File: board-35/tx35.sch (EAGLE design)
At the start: 23 parts, among them J1 SWD_SHROUD, Q1 MOSFET-NCHANNEL2N7002PW, X1 SMA-142-0711-821/826

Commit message: almost done 35mhz tranasmitter
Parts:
- added C13: (no value), passives-7351:CAPACITOR0805-N
- added JP1: (no value), Mine:M02PTH
- added JP2: (no value), SparkFun-Connectors:M06SILK_FEMALE_PTH
- added R4: 10k, passives-7351:RESISTOR0603-N
- IC1: value STM32F0-32 -> STM32F030K6
- renumbered U$1 to IC1
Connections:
- new net N$12: IC1.PA9, JP2.5
- new net N$13: IC1.BOOT0, JP1.1, R4.P$1
- new net N$7: C13.1, JP2.2, L1.P$2
- new net N$9: IC1.PA10, JP2.4
- net +3V3: now also JP1.2, JP2.3
- net GND: now also C13.2, JP2.1, R4.P$2
- net N$5: now also JP2.6
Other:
- note added: "analogue in/out"
- note added: "control in"
- note added: "en"
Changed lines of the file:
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@@
 <?xml version="1.0" encoding="utf-8"?>
 <!DOCTYPE eagle SYSTEM "eagle.dtd">
-<eagle version="6.5.0">
+<eagle version="6.6.0">
 <drawing>
 <settings>
@@
 </classes>
 <parts>
-<part name="U$1" library="Mine" deviceset="STM32F0-32" device=""/>
+<part name="IC1" library="Mine" deviceset="STM32F0-32" device="" value="STM32F030K6"/>
 <part name="Y1" library="SparkFun-FreqCtrl" deviceset="CRYSTAL" device="HC49UV"/>
 <part name="C1" library="passives-7351" deviceset="CAPACITOR" device="0603-N" value="18p"/>
@@
 <part name="GND10" library="supply1" deviceset="GND" device=""/>
 <part name="GND11" library="supply1" deviceset="GND" device=""/>
+<part name="+3V3" library="supply1" deviceset="+3V3" device=""/>
+<part name="GND12" library="supply1" deviceset="GND" device=""/>
+<part name="JP2" library="SparkFun-Connectors" deviceset="M06" device="SILK_FEMALE_PTH"/>
+<part name="R4" library="passives-7351" deviceset="RESISTOR" device="0603-N" value="10k"/>
+<part name="GND13" library="supply1" deviceset="GND" device=""/>
+<part name="JP1" library="Mine" deviceset="M02" device="PTH"/>
+<part name="+3V4" library="supply1" deviceset="+3V3" device=""/>
+<part name="C13" library="passives-7351" deviceset="CAPACITOR" device="0805-N"/>
+<part name="GND14" library="supply1" deviceset="GND" device=""/>
 </parts>
 <sheets>
@@
 <text x="114.3" y="66.04" size="1.778" layer="91">CHECK</text>
 <text x="104.14" y="60.96" size="1.778" layer="91">CHECK</text>
+<text x="78.74" y="139.7" size="1.778" layer="91">analogue in/out</text>
+<text x="78.74" y="134.62" size="1.778" layer="91">control in</text>
+<text x="78.74" y="137.16" size="1.778" layer="91">en</text>
 </plain>
 <instances>
-<instance part="U$1" gate="G$1" x="50.8" y="25.4"/>
+<instance part="IC1" gate="G$1" x="50.8" y="25.4"/>
 <instance part="Y1" gate="G$1" x="96.52" y="10.16" rot="R180"/>
 <instance part="C1" gate="G$1" x="91.44" y="2.54"/>
@@
 <instance part="GND10" gate="1" x="175.26" y="55.88"/>
 <instance part="GND11" gate="1" x="187.96" y="58.42"/>
+<instance part="+3V3" gate="G$1" x="76.2" y="132.08" rot="R270"/>
+<instance part="GND12" gate="1" x="76.2" y="121.92"/>
+<instance part="JP2" gate="G$1" x="68.58" y="132.08"/>
+<instance part="R4" gate="G$1" x="10.16" y="48.26" rot="R270"/>
+<instance part="GND13" gate="1" x="10.16" y="40.64"/>
+<instance part="JP1" gate="G$1" x="-10.16" y="53.34"/>
+<instance part="+3V4" gate="G$1" x="0" y="55.88" rot="R270"/>
+<instance part="C13" gate="G$1" x="127" y="88.9"/>
+<instance part="GND14" gate="1" x="127" y="81.28"/>
 </instances>
 <busses>
@@
 <net name="N$1" class="0">
 <segment>
-<pinref part="U$1" gate="G$1" pin="PF1"/>
+<pinref part="IC1" gate="G$1" pin="PF1"/>
 <wire x1="83.82" y1="10.16" x2="88.9" y2="10.16" width="0.1524" layer="91"/>
 <wire x1="88.9" y1="10.16" x2="88.9" y2="15.24" width="0.1524" layer="91"/>
@@
 <net name="N$2" class="0">
 <segment>
-<pinref part="U$1" gate="G$1" pin="PF0"/>
+<pinref part="IC1" gate="G$1" pin="PF0"/>
 <pinref part="C1" gate="G$1" pin="1"/>
 <wire x1="83.82" y1="12.7" x2="91.44" y2="12.7" width="0.1524" layer="91"/>
@@
 <wire x1="17.78" y1="22.86" x2="22.86" y2="22.86" width="0.1524" layer="91"/>
 <wire x1="22.86" y1="22.86" x2="22.86" y2="25.4" width="0.1524" layer="91"/>
-<pinref part="U$1" gate="G$1" pin="VSS1"/>
+<pinref part="IC1" gate="G$1" pin="VSS1"/>
 <wire x1="25.4" y1="20.32" x2="22.86" y2="20.32" width="0.1524" layer="91"/>
 <wire x1="22.86" y1="20.32" x2="22.86" y2="22.86" width="0.1524" layer="91"/>
-<pinref part="U$1" gate="G$1" pin="VSS"/>
+<pinref part="IC1" gate="G$1" pin="VSS"/>
 <wire x1="22.86" y1="22.86" x2="25.4" y2="22.86" width="0.1524" layer="91"/>
 <junction x="22.86" y="22.86"/>
@@
 <wire x1="187.96" y1="66.04" x2="187.96" y2="60.96" width="0.1524" layer="91"/>
 </segment>
+<segment>
+<pinref part="GND12" gate="1" pin="GND"/>
+<wire x1="73.66" y1="127" x2="76.2" y2="127" width="0.1524" layer="91"/>
+<wire x1="76.2" y1="127" x2="76.2" y2="124.46" width="0.1524" layer="91"/>
+<pinref part="JP2" gate="G$1" pin="1"/>
+</segment>
+<segment>
+<pinref part="R4" gate="G$1" pin="P$2"/>
+<pinref part="GND13" gate="1" pin="GND"/>
+</segment>
+<segment>
+<pinref part="C13" gate="G$1" pin="2"/>
+<pinref part="GND14" gate="1" pin="GND"/>
+</segment>
 </net>
 <net name="N$5" class="0">
 <segment>
-<pinref part="U$1" gate="G$1" pin="PB5"/>
-<wire x1="83.82" y1="22.86" x2="137.16" y2="22.86" width="0.1524" layer="91"/>
+<pinref part="IC1" gate="G$1" pin="PB5"/>
+<wire x1="83.82" y1="22.86" x2="104.14" y2="22.86" width="0.1524" layer="91"/>
+<wire x1="104.14" y1="22.86" x2="137.16" y2="22.86" width="0.1524" layer="91"/>
 <wire x1="137.16" y1="22.86" x2="137.16" y2="10.16" width="0.1524" layer="91"/>
 <pinref part="R2" gate="G$1" pin="P$1"/>
 <wire x1="137.16" y1="10.16" x2="134.62" y2="10.16" width="0.1524" layer="91"/>
+<wire x1="104.14" y1="22.86" x2="104.14" y2="132.08" width="0.1524" layer="91"/>
+<junction x="104.14" y="22.86"/>
+<pinref part="JP2" gate="G$1" pin="6"/>
+<wire x1="104.14" y1="132.08" x2="104.14" y2="134.62" width="0.1524" layer="91"/>
+<wire x1="73.66" y1="139.7" x2="104.14" y2="139.7" width="0.1524" layer="91"/>
+<wire x1="104.14" y1="139.7" x2="104.14" y2="134.62" width="0.1524" layer="91"/>
 </segment>
 </net>
@@
 <pinref part="+3V1" gate="G$1" pin="+3V3"/>
 <wire x1="20.32" y1="43.18" x2="20.32" y2="40.64" width="0.1524" layer="91"/>
-<pinref part="U$1" gate="G$1" pin="VDD"/>
+<pinref part="IC1" gate="G$1" pin="VDD"/>
 <wire x1="20.32" y1="40.64" x2="20.32" y2="35.56" width="0.1524" layer="91"/>
 <wire x1="20.32" y1="35.56" x2="22.86" y2="35.56" width="0.1524" layer="91"/>
-<pinref part="U$1" gate="G$1" pin="VDD1"/>
+<pinref part="IC1" gate="G$1" pin="VDD1"/>
 <wire x1="22.86" y1="35.56" x2="25.4" y2="35.56" width="0.1524" layer="91"/>
 <wire x1="25.4" y1="33.02" x2="22.86" y2="33.02" width="0.1524" layer="91"/>
@@
 <wire x1="12.7" y1="33.02" x2="12.7" y2="35.56" width="0.1524" layer="91"/>
 <wire x1="12.7" y1="35.56" x2="17.78" y2="35.56" width="0.1524" layer="91"/>
-<pinref part="U$1" gate="G$1" pin="VDDA"/>
+<pinref part="IC1" gate="G$1" pin="VDDA"/>
 <wire x1="25.4" y1="40.64" x2="20.32" y2="40.64" width="0.1524" layer="91"/>
 <junction x="17.78" y="35.56"/>
@@
 <pinref part="+3V2" gate="G$1" pin="+3V3"/>
 </segment>
+<segment>
+<pinref part="JP1" gate="G$1" pin="2"/>
+<pinref part="+3V4" gate="G$1" pin="+3V3"/>
+</segment>
+<segment>
+<pinref part="+3V3" gate="G$1" pin="+3V3"/>
+<pinref part="JP2" gate="G$1" pin="3"/>
+</segment>
 </net>
 <net name="NRST" class="0">
 <segment>
-<pinref part="U$1" gate="G$1" pin="NRST"/>
+<pinref part="IC1" gate="G$1" pin="NRST"/>
 <wire x1="25.4" y1="58.42" x2="17.78" y2="58.42" width="0.1524" layer="91"/>
 <label x="17.78" y="58.42" size="1.778" layer="95"/>
@@
 <net name="SWDIO" class="0">
 <segment>
-<pinref part="U$1" gate="G$1" pin="PA13"/>
+<pinref part="IC1" gate="G$1" pin="PA13"/>
 <wire x1="83.82" y1="48.26" x2="93.98" y2="48.26" width="0.1524" layer="91"/>
 <label x="88.9" y="48.26" size="1.778" layer="95"/>
@@
 <net name="SWDCLK" class="0">
 <segment>
-<pinref part="U$1" gate="G$1" pin="PA14"/>
+<pinref part="IC1" gate="G$1" pin="PA14"/>
 <wire x1="83.82" y1="45.72" x2="93.98" y2="45.72" width="0.1524" layer="91"/>
 <label x="88.9" y="45.72" size="1.778" layer="95"/>
@@
 <net name="MCO" class="0">
 <segment>
-<pinref part="U$1" gate="G$1" pin="PA8"/>
+<pinref part="IC1" gate="G$1" pin="PA8"/>
 <wire x1="83.82" y1="60.96" x2="114.3" y2="60.96" width="0.1524" layer="91"/>
 <label x="88.9" y="60.96" size="1.778" layer="95"/>
@@
 </segment>
 </net>
+<net name="N$7" class="0">
+<segment>
+<pinref part="L1" gate="G$1" pin="P$2"/>
+<pinref part="JP2" gate="G$1" pin="2"/>
+<wire x1="121.92" y1="129.54" x2="121.92" y2="93.98" width="0.1524" layer="91"/>
+<wire x1="121.92" y1="93.98" x2="121.92" y2="81.28" width="0.1524" layer="91"/>
+<wire x1="73.66" y1="129.54" x2="121.92" y2="129.54" width="0.1524" layer="91"/>
+<pinref part="C13" gate="G$1" pin="1"/>
+<wire x1="127" y1="91.44" x2="127" y2="93.98" width="0.1524" layer="91"/>
+<wire x1="127" y1="93.98" x2="121.92" y2="93.98" width="0.1524" layer="91"/>
+<junction x="121.92" y="93.98"/>
+</segment>
+</net>
+<net name="N$9" class="0">
+<segment>
+<pinref part="IC1" gate="G$1" pin="PA10"/>
+<wire x1="83.82" y1="55.88" x2="101.6" y2="55.88" width="0.1524" layer="91"/>
+<wire x1="101.6" y1="55.88" x2="101.6" y2="134.62" width="0.1524" layer="91"/>
+<pinref part="JP2" gate="G$1" pin="4"/>
+<wire x1="73.66" y1="134.62" x2="101.6" y2="134.62" width="0.1524" layer="91"/>
+</segment>
+</net>
+<net name="N$12" class="0">
+<segment>
+<pinref part="IC1" gate="G$1" pin="PA9"/>
+<wire x1="83.82" y1="58.42" x2="99.06" y2="58.42" width="0.1524" layer="91"/>
+<wire x1="99.06" y1="58.42" x2="99.06" y2="127" width="0.1524" layer="91"/>
+<pinref part="JP2" gate="G$1" pin="5"/>
+<wire x1="99.06" y1="127" x2="99.06" y2="129.54" width="0.1524" layer="91"/>
+<wire x1="73.66" y1="137.16" x2="99.06" y2="137.16" width="0.1524" layer="91"/>
+<wire x1="99.06" y1="137.16" x2="99.06" y2="129.54" width="0.1524" layer="91"/>
+</segment>
+</net>
+<net name="N$13" class="0">
+<segment>
+<pinref part="IC1" gate="G$1" pin="BOOT0"/>
+<wire x1="25.4" y1="53.34" x2="10.16" y2="53.34" width="0.1524" layer="91"/>
+<pinref part="R4" gate="G$1" pin="P$1"/>
+<junction x="10.16" y="53.34"/>
+<wire x1="10.16" y1="53.34" x2="-2.54" y2="53.34" width="0.1524" layer="91"/>
+<pinref part="JP1" gate="G$1" pin="1"/>
+</segment>
+</net>

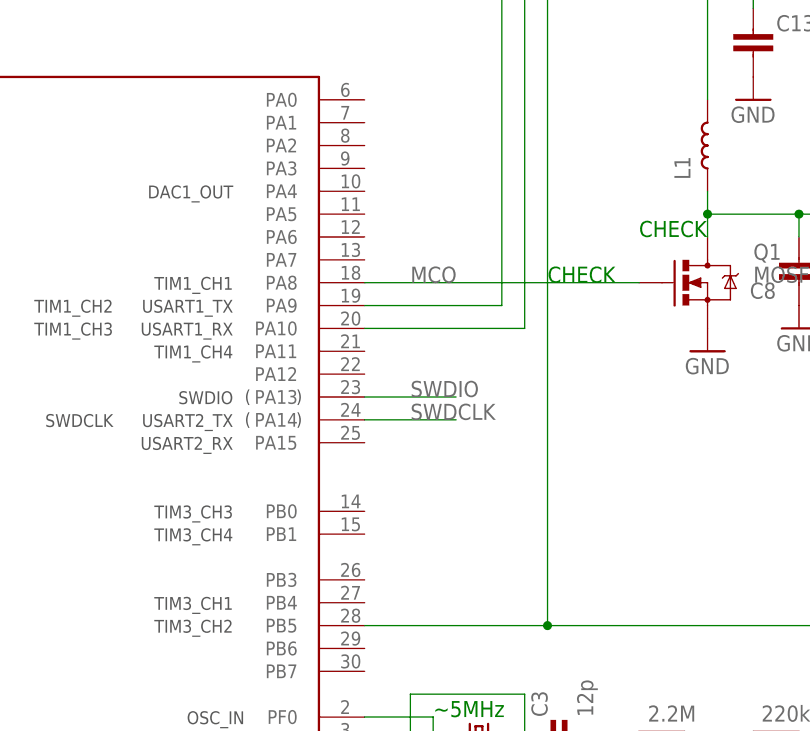
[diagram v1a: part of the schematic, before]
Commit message: adding some mire testpads
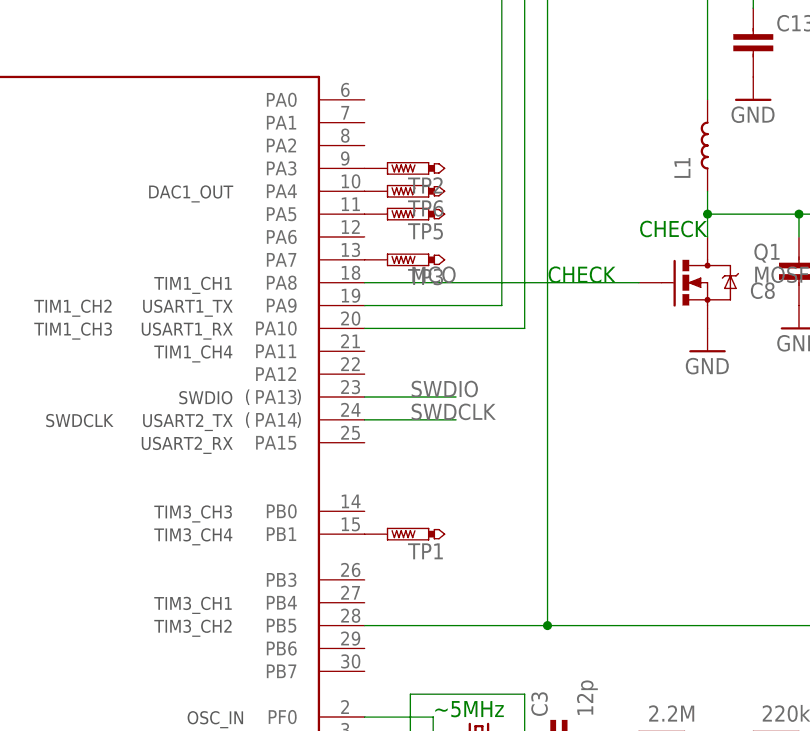
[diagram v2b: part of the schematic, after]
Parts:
- added TP1, TP2, TP3, TP5, TP6: PTR1TP11R, testpad:PTR1TP11R
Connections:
- new net N$14: IC1.PA3, TP2.TP
- new net N$15: IC1.PB1, TP1.TP
- new net N$16: IC1.PA7, TP3.TP
- new net N$18: IC1.PA5, TP5.TP
- new net N$19: IC1.PA4, TP6.TP
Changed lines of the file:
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@@
 <part name="C13" library="passives-7351" deviceset="CAPACITOR" device="0805-N"/>
 <part name="GND14" library="supply1" deviceset="GND" device=""/>
+<part name="TP1" library="testpad" deviceset="PTR1" device="TP11R"/>
+<part name="TP3" library="testpad" deviceset="PTR1" device="TP11R"/>
+<part name="TP5" library="testpad" deviceset="PTR1" device="TP11R"/>
+<part name="TP6" library="testpad" deviceset="PTR1" device="TP11R"/>
+<part name="TP2" library="testpad" deviceset="PTR1" device="TP11R"/>
 </parts>
 <sheets>
@@
 <instance part="C13" gate="G$1" x="127" y="88.9"/>
 <instance part="GND14" gate="1" x="127" y="81.28"/>
+<instance part="TP1" gate="G$1" x="86.36" y="33.02" rot="R90"/>
+<instance part="TP3" gate="G$1" x="86.36" y="63.5" rot="R90"/>
+<instance part="TP5" gate="G$1" x="86.36" y="68.58" rot="R90"/>
+<instance part="TP6" gate="G$1" x="86.36" y="71.12" rot="R90"/>
+<instance part="TP2" gate="G$1" x="86.36" y="73.66" rot="R90"/>
 </instances>
 <busses>
@@
 </segment>
 </net>
+<net name="N$15" class="0">
+<segment>
+<pinref part="IC1" gate="G$1" pin="PB1"/>
+<pinref part="TP1" gate="G$1" pin="TP"/>
+</segment>
+</net>
+<net name="N$16" class="0">
+<segment>
+<pinref part="IC1" gate="G$1" pin="PA7"/>
+<pinref part="TP3" gate="G$1" pin="TP"/>
+</segment>
+</net>
+<net name="N$18" class="0">
+<segment>
+<pinref part="IC1" gate="G$1" pin="PA5"/>
+<pinref part="TP5" gate="G$1" pin="TP"/>
+</segment>
+</net>
+<net name="N$19" class="0">
+<segment>
+<pinref part="IC1" gate="G$1" pin="PA4"/>
+<pinref part="TP6" gate="G$1" pin="TP"/>
+</segment>
+</net>
+<net name="N$14" class="0">
+<segment>
+<pinref part="IC1" gate="G$1" pin="PA3"/>
+<pinref part="TP2" gate="G$1" pin="TP"/>
+</segment>
+</net>

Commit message: addin gvalues
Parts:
- D1: FARNELL (none) -> 1757783/(2443453)
- IC1: FARNELL (none) -> 2432085
- L1: value (none) -> 2u2; FARNELL (none) -> 2215642
- L2: FARNELL (none) -> 1669538/(1711879)
- Q1: FARNELL (none) -> 9845313
- Y1: FARNELL (none) -> 1666962/(1652566)
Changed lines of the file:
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@@
 </classes>
 <parts>
-<part name="IC1" library="Mine" deviceset="STM32F0-32" device="" value="STM32F030K6"/>
-<part name="Y1" library="SparkFun-FreqCtrl" deviceset="CRYSTAL" device="HC49UV"/>
+<part name="IC1" library="Mine" deviceset="STM32F0-32" device="" value="STM32F030K6">
+<attribute name="FARNELL" value="2432085"/>
+</part>
+<part name="Y1" library="SparkFun-FreqCtrl" deviceset="CRYSTAL" device="HC49UV">
+<attribute name="FARNELL" value="1666962/(1652566)"/>
+</part>
 <part name="C1" library="passives-7351" deviceset="CAPACITOR" device="0603-N" value="18p"/>
 <part name="C2" library="passives-7351" deviceset="CAPACITOR" device="0603-N" value="12p"/>
 <part name="C3" library="passives-7351" deviceset="CAPACITOR" device="0603-N" value="12p"/>
 <part name="C4" library="passives-7351" deviceset="CAPACITOR" device="0603-N" value="560p"/>
-<part name="D1" library="diode" deviceset="DIODE_CAPACITANCE-" device="SOD523"/>
+<part name="D1" library="diode" deviceset="DIODE_CAPACITANCE-" device="SOD523">
+<attribute name="FARNELL" value="1757783/(2443453)"/>
+</part>
 <part name="R1" library="passives-7351" deviceset="RESISTOR" device="0603-N" value="2.2M"/>
 <part name="R2" library="passives-7351" deviceset="RESISTOR" device="0603-N" value="220k"/>
@@
 <part name="+3V2" library="supply1" deviceset="+3V3" device=""/>
 <part name="GND6" library="supply1" deviceset="GND" device=""/>
-<part name="Q1" library="SparkFun-DiscreteSemi" deviceset="MOSFET-NCHANNEL" device="2N7002PW"/>
-<part name="L1" library="passives-7351" deviceset="INDUCTOR" device="0603-N"/>
+<part name="Q1" library="SparkFun-DiscreteSemi" deviceset="MOSFET-NCHANNEL" device="2N7002PW">
+<attribute name="FARNELL" value="9845313"/>
+</part>
+<part name="L1" library="passives-7351" deviceset="INDUCTOR" device="0603-N" value="2u2">
+<attribute name="FARNELL" value="2215642"/>
+</part>
 <part name="C8" library="passives-7351" deviceset="CAPACITOR" device="0603-N"/>
 <part name="C9" library="passives-7351" deviceset="CAPACITOR" device="0603-N"/>
-<part name="L2" library="passives-7351" deviceset="INDUCTOR" device="0603-N"/>
+<part name="L2" library="passives-7351" deviceset="INDUCTOR" device="0603-N">
+<attribute name="FARNELL" value="1669538/(1711879)"/>
+</part>
 <part name="C10" library="passives-7351" deviceset="CAPACITOR" device="0603-N"/>
 <part name="L3" library="passives-7351" deviceset="INDUCTOR" device="0603-N"/>
@@
 </plain>
 <instances>
-<instance part="IC1" gate="G$1" x="50.8" y="25.4"/>
-<instance part="Y1" gate="G$1" x="96.52" y="10.16" rot="R180"/>
+<instance part="IC1" gate="G$1" x="50.8" y="25.4">
+<attribute name="FARNELL" x="50.8" y="25.4" size="1.778" layer="96" display="off"/>
+</instance>
+<instance part="Y1" gate="G$1" x="96.52" y="10.16" rot="R180">
+<attribute name="FARNELL" x="96.52" y="10.16" size="1.778" layer="96" rot="R180" display="off"/>
+</instance>
 <instance part="C1" gate="G$1" x="91.44" y="2.54"/>
 <instance part="C2" gate="G$1" x="101.6" y="2.54"/>
 <instance part="C3" gate="G$1" x="104.14" y="10.16" rot="R90"/>
 <instance part="C4" gate="G$1" x="121.92" y="0" rot="R180"/>
-<instance part="D1" gate="-B1" x="111.76" y="2.54" rot="R90"/>
+<instance part="D1" gate="-B1" x="111.76" y="2.54" rot="R90">
+<attribute name="FARNELL" x="111.76" y="2.54" size="1.778" layer="96" rot="R90" display="off"/>
+</instance>
 <instance part="R1" gate="G$1" x="116.84" y="10.16" rot="R180"/>
 <instance part="R2" gate="G$1" x="129.54" y="10.16" rot="R180"/>
@@
 <instance part="+3V2" gate="G$1" x="35.56" y="111.76"/>
 <instance part="GND6" gate="1" x="35.56" y="91.44"/>
-<instance part="Q1" gate="G$1" x="121.92" y="60.96"/>
-<instance part="L1" gate="G$1" x="121.92" y="76.2" rot="R90"/>
+<instance part="Q1" gate="G$1" x="121.92" y="60.96">
+<attribute name="FARNELL" x="121.92" y="60.96" size="1.778" layer="96" display="off"/>
+</instance>
+<instance part="L1" gate="G$1" x="121.92" y="76.2" rot="R90">
+<attribute name="FARNELL" x="121.92" y="76.2" size="1.778" layer="96" rot="R90" display="off"/>
+</instance>
 <instance part="C8" gate="G$1" x="132.08" y="60.96" rot="R180"/>
 <instance part="C9" gate="G$1" x="152.4" y="68.58" rot="R270"/>
-<instance part="L2" gate="G$1" x="139.7" y="68.58"/>
+<instance part="L2" gate="G$1" x="139.7" y="68.58">
+<attribute name="FARNELL" x="139.7" y="68.58" size="1.778" layer="96" display="off"/>
+</instance>
 <instance part="C10" gate="G$1" x="160.02" y="63.5"/>
 <instance part="L3" gate="G$1" x="167.64" y="68.58"/>

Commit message: updating some ording numbers
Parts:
- C8: FARNELL (none) -> 2434613/2435457
- Q1: FARNELL 9845313 -> 1894713
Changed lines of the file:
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@@
 <?xml version="1.0" encoding="utf-8"?>
 <!DOCTYPE eagle SYSTEM "eagle.dtd">
-<eagle version="6.6.0">
+<eagle version="6.5.0">
 <drawing>
 <settings>
@@
 <part name="GND6" library="supply1" deviceset="GND" device=""/>
 <part name="Q1" library="SparkFun-DiscreteSemi" deviceset="MOSFET-NCHANNEL" device="2N7002PW">
-<attribute name="FARNELL" value="9845313"/>
+<attribute name="FARNELL" value="1894713"/>
 </part>
 <part name="L1" library="passives-7351" deviceset="INDUCTOR" device="0603-N" value="2u2">
 <attribute name="FARNELL" value="2215642"/>
 </part>
-<part name="C8" library="passives-7351" deviceset="CAPACITOR" device="0603-N"/>
+<part name="C8" library="passives-7351" deviceset="CAPACITOR" device="0603-N">
+<attribute name="FARNELL" value="2434613/2435457"/>
+</part>
 <part name="C9" library="passives-7351" deviceset="CAPACITOR" device="0603-N"/>
 <part name="L2" library="passives-7351" deviceset="INDUCTOR" device="0603-N">
@@
 <attribute name="FARNELL" x="121.92" y="76.2" size="1.778" layer="96" rot="R90" display="off"/>
 </instance>
-<instance part="C8" gate="G$1" x="132.08" y="60.96" rot="R180"/>
+<instance part="C8" gate="G$1" x="132.08" y="60.96" rot="R180">
+<attribute name="FARNELL" x="132.08" y="60.96" size="1.778" layer="96" rot="R180" display="off"/>
+</instance>
 <instance part="C9" gate="G$1" x="152.4" y="68.58" rot="R270"/>
 <instance part="L2" gate="G$1" x="139.7" y="68.58">
